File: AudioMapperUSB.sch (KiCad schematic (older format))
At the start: 98 parts, among them J1 USB_B, J10 Conn_01x01, J11 Conn_01x01, J2 Audio-Jack-2, J3 Conn_01x02, J4 Audio-Jack-2, J5 Conn_01x02, J6 Conn_01x02, J7 Conn_01x02, J8 Conn_01x01, J9 Conn_01x01, Q1 SS8550, U1 AMS1117-3.3, U2 PCM2900, U3 OPA2170, U4 OPA2170, U5 OPA2170, Y1 12 MHz

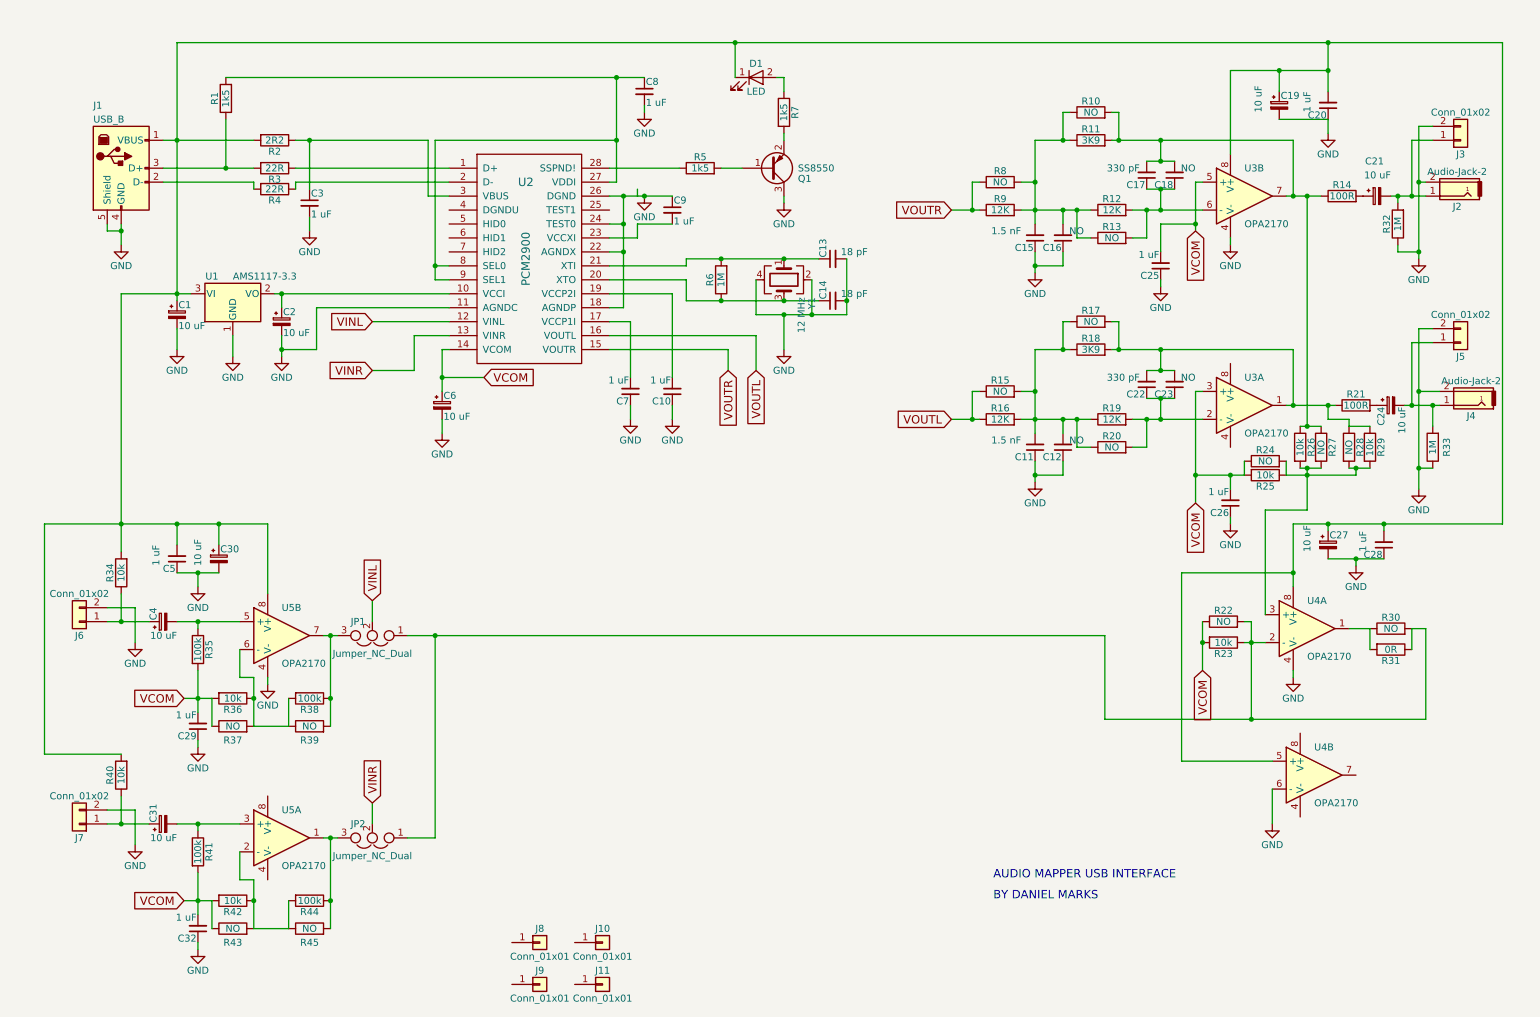
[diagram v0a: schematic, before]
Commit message: Added second gain stage to microphone
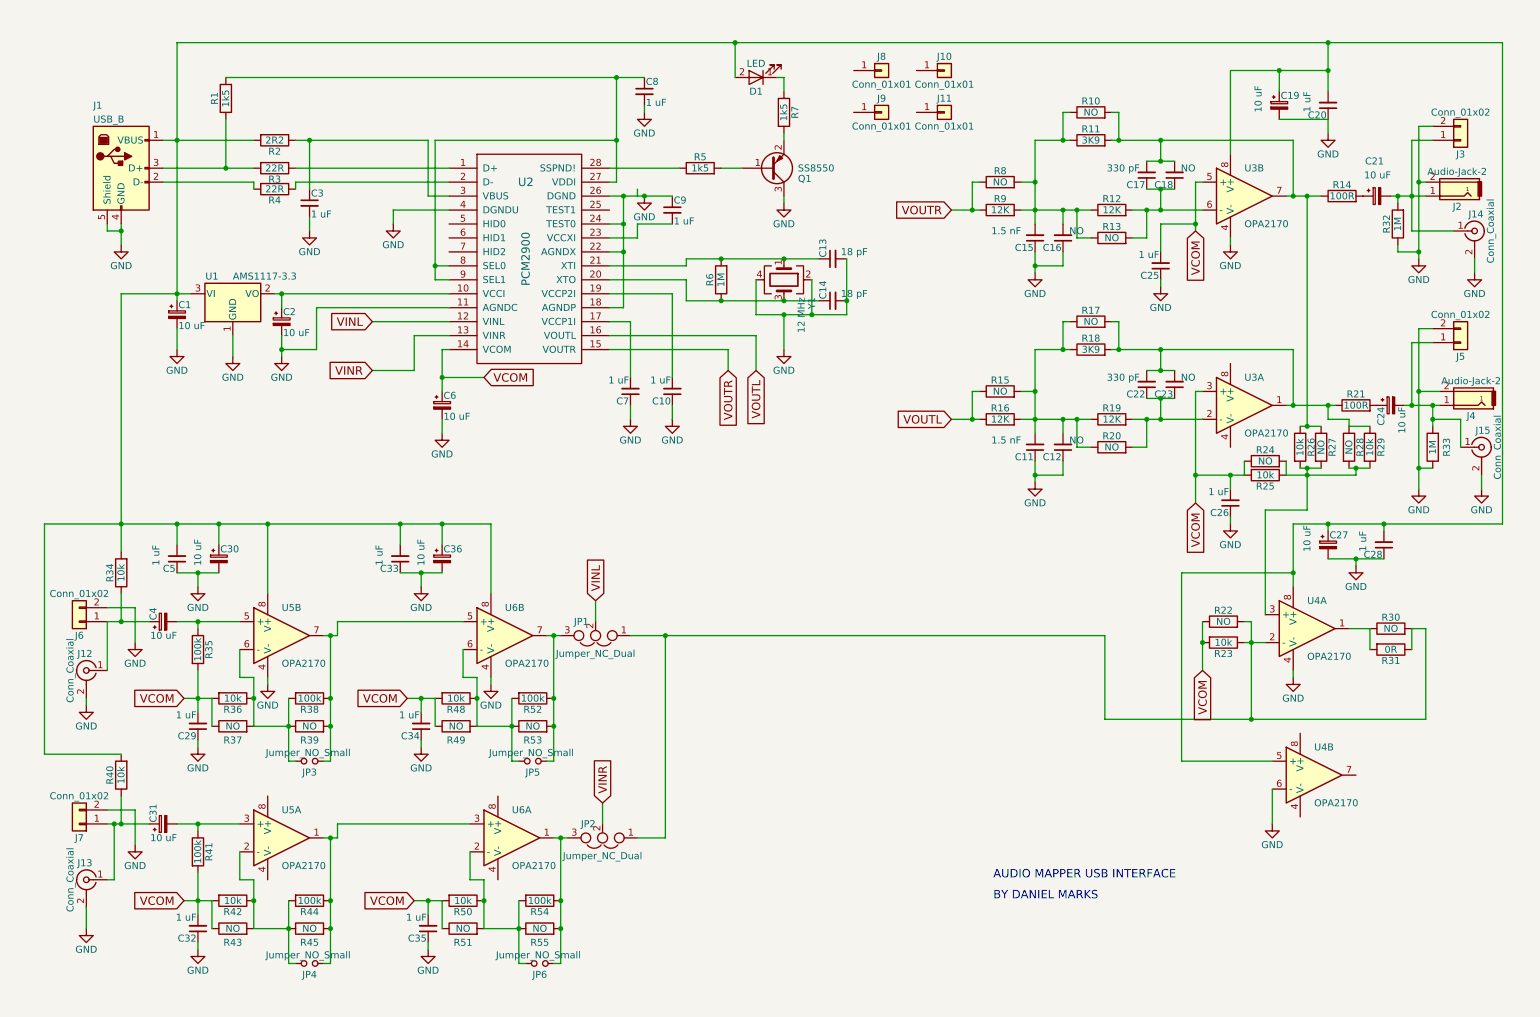
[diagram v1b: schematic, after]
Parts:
- added C33, C34, C35: 1 uF, Capacitors_SMD:C_0805_HandSoldering, symbol C_Small
- added C36: 10 uF, AudioMapperUSB:CP_1206_HandSoldering, symbol CP_Small
- added J12, J13, J14, J15: Conn_Coaxial, Connectors:SMA_THT_Jack_Straight, symbol Conn_Coaxial
- added JP3, JP4, JP5, JP6: Jumper_NO_Small, Pin_Headers:Pin_Header_Straight_1x02_Pitch2.54mm, symbol Jumper_NO_Small
- added R48, R50: 10k, Resistors_SMD:R_0805_HandSoldering, symbol R
- added R49, R51, R53, R55: NO, Resistors_THT:R_Axial_DIN0207_L6.3mm_D2.5mm_P7.62mm_Horizontal, symbol R
- added R52, R54: 100k, Resistors_SMD:R_0805_HandSoldering, symbol R
- added U6: OPA2170, Housings_SOIC:SOIC-8_3.9x4.9mm_Pitch1.27mm, symbol LM358
- C1, C19, C2, C21, C24, C27, C30, C31, C4, C6: footprint Capacitors_SMD:C_1206_HandSoldering -> AudioMapperUSB:CP_1206_HandSoldering
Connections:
- net GND: now also U2.4 (DGNDU), C33.1, C34.1, C35.1, C36.2, J12.2 (Ext), J13.2 (Ext), J14.2 (Ext), J15.2 (Ext), U6.4 (V-)
- net VCOM: now also C34.2, C35.2, R48.2, R49.1, R50.2, R51.1
- net at C1.1, C19.1, C20.2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: now also D1.2 (A), C33.2, C36.1, U6.8 (V+); no longer D1.1 (K)
- net at C4.1, J6.1 (Pin_1), R34.1: now also J12.1 (In)
- net at C24.2, J4.1, J5.1 (Pin_1)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: now also J15.1 (In)
- net at C21.2, J2.1, J3.1 (Pin_1)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: now also J14.1 (In)
- net at R7.1: now also D1.1 (K); no longer D1.2 (A)
- net at R36.1, R37.2, R38.2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: now also JP3.2
- net at R38.1, R39.2, U5.7: now also JP3.1, U6.5 (+); no longer JP1.3
- net at C31.1, J7.1 (Pin_1), R40.1: now also J13.1 (In)
- net at R44.1, R45.2, U5.1: now also JP4.1, U6.3 (+); no longer JP2.3
- net at R42.1, R43.2, R44.2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: now also JP4.2
- new net: JP1.3, JP5.1, R52.1, R53.2, U6.7
- new net: JP2.3, JP6.1, R54.1, R55.2, U6.1
- new net: JP6.2, R50.1, R51.2, R54.2, R55.1, U6.2 (-)
- new net: JP5.2, R48.1, R49.2, R52.2, R53.1, U6.6 (-)
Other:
- moved on the sheet: D1, J10, J11, J8, J9, JP1, JP2

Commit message: Added antialiasing on input and SP/DIF input/output
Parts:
- added C37, C38, C39, C40: 22 pF, Capacitors_SMD:C_0805_HandSoldering, symbol C_Small
- added J16, J17: Audio-Jack-2, AudioMapperUSB:RCAConnectorCommon, symbol Audio-Jack-2
- added JP7: Jumper_NC_Small, Pin_Headers:Pin_Header_Straight_1x02_Pitch2.54mm, symbol Jumper_NC_Small
- R11: value 3K9 -> 12K; LCSC C17614 -> C17444
- R12, R19: value 12K -> 3k9; LCSC C17444 -> C17614
- R18: value 3K9 -> 12K
- R36, R42, R48, R50: value 10k -> 4k7; LCSC C17414 -> C17673
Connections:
- net GND: now also C9.2, J16.2, J17.2, JP7.1; no longer C9.1, U2.24 (TEST0)
- net at U2.23 (VCCXI): now also C9.1; no longer C9.2
- net at U2.25 (TEST1): now also J16.1
- net at JP3.2, R36.1, R37.2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: now also C37.1
- net at JP3.1, R38.1, R39.2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: now also C37.2
- net at JP1.3, JP5.1, R52.1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: now also C39.2
- net at JP4.1, R44.1, R45.2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: now also C38.2
- net at JP4.2, R42.1, R43.2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: now also C38.1
- net at JP2.3, JP6.1, R54.1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: now also C40.2
- net at JP6.2, R50.1, R51.2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: now also C40.1
- net at JP5.2, R48.1, R49.2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: now also C39.1
- new net: J17.1, JP7.2, U2.24 (TEST0)
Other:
- moved on the sheet: C9, D1, Q1, R5, R7

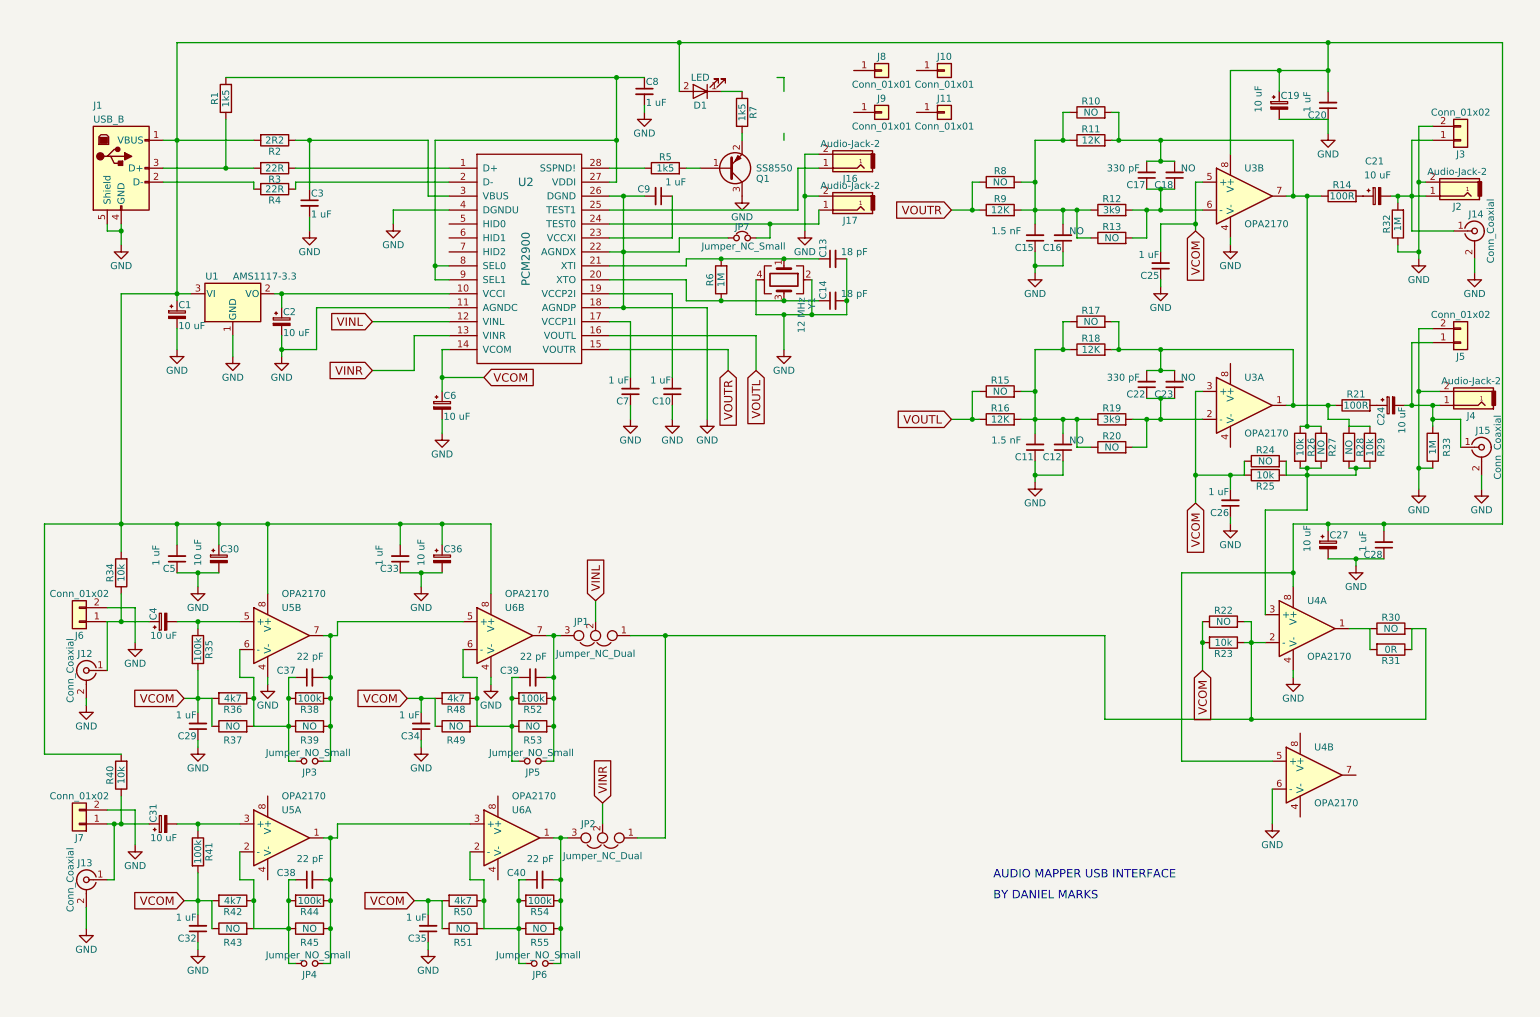
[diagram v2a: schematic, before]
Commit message: Added ability to chain outputs of two boards together
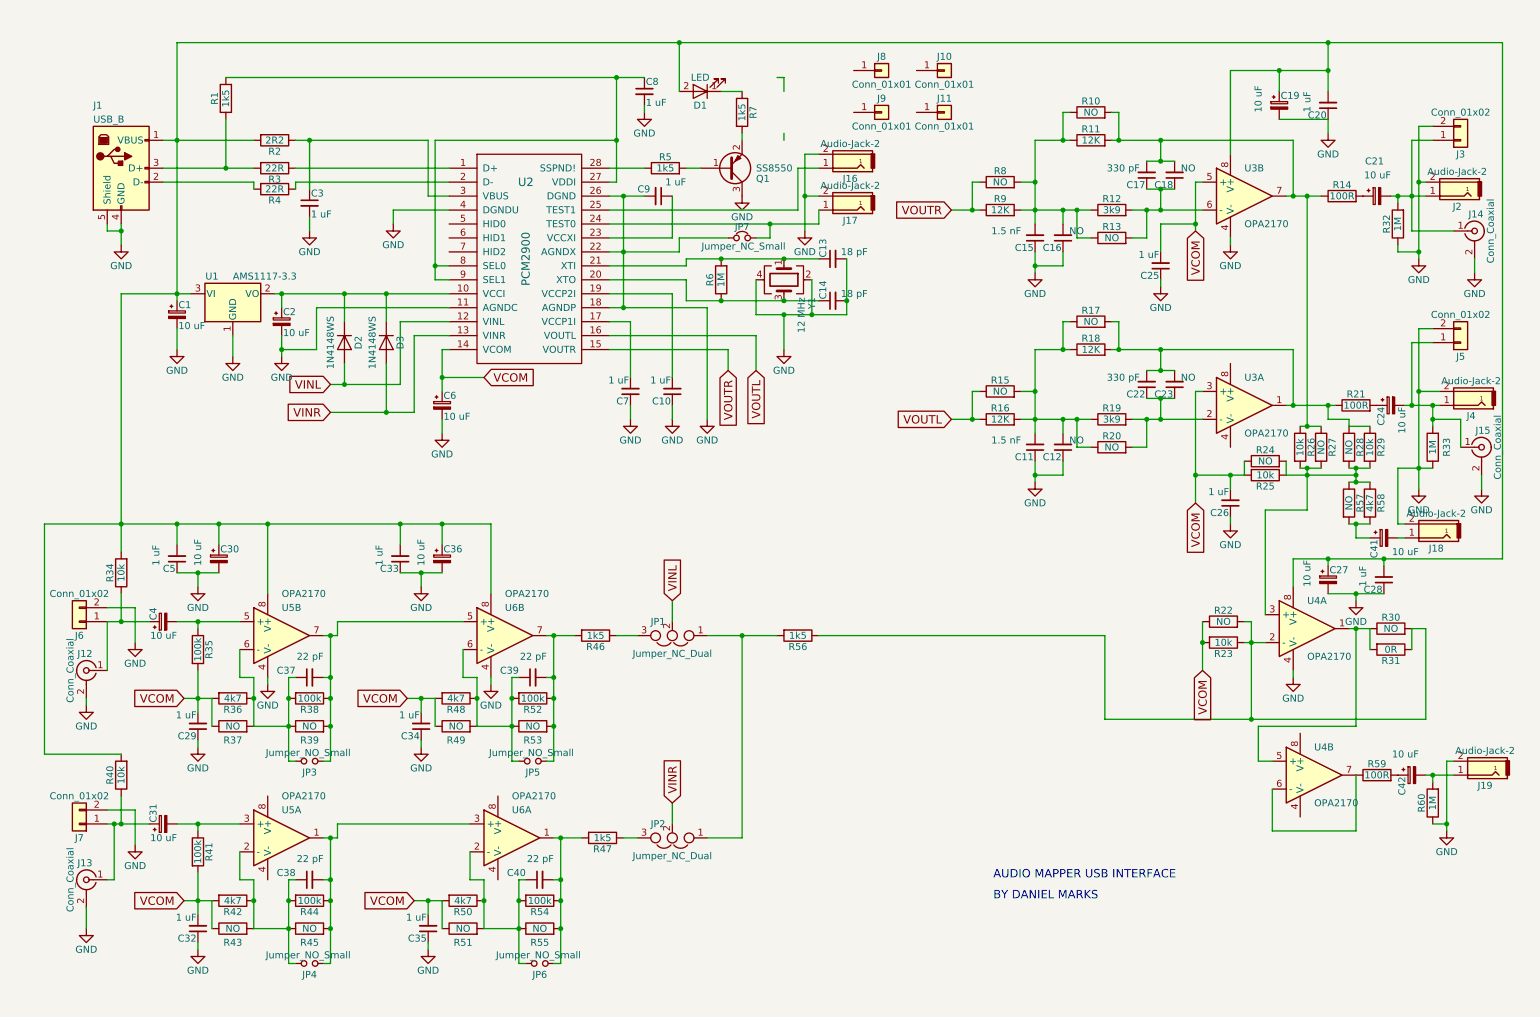
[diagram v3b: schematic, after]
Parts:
- added C41, C42: 10 uF, AudioMapperUSB:CP_1206_HandSoldering, symbol CP_Small
- added D2, D3: 1N4148WS, Diodes_SMD:D_SOD-323_HandSoldering, symbol D
- added J18, J19: Audio-Jack-2, AudioMapperUSB:RCAConnectorCommon, symbol Audio-Jack-2
- added R46, R47, R56: 1k5, Resistors_SMD:R_0805_HandSoldering, symbol R
- added R57: NO, Resistors_THT:R_Axial_DIN0207_L6.3mm_D2.5mm_P7.62mm_Horizontal, symbol R
- added R58: 4k7, Resistors_SMD:R_0805_HandSoldering, symbol R
- added R59: 100R, Resistors_SMD:R_0805_HandSoldering, symbol R
- added R60: 1M, Resistors_SMD:R_0805_HandSoldering, symbol R
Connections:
- net GND: now also J18.2, J19.2, R60.1; no longer U4.6 (-)
- net VINL: now also D2.2 (A)
- net VINR: now also D3.2 (A)
- net at C2.1, U1.2 (VO), U2.10 (VCCI): now also D2.1 (K), D3.1 (K)
- net at C1.1, C19.1, C20.2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: no longer U4.5 (+)
- net at U4.7: now also U4.6 (-), R59.1
- net at R30.1, R31.2, U4.1: now also U4.5 (+)
- net at R22.2, R23.1, R30.2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: now also R56.1; no longer JP1.1, JP2.1
- net at R24.2, R25.1, R26.2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: now also R57.1, R58.1
- net at C39.2, JP5.1, R52.1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: now also R46.2; no longer JP1.3
- net at C40.2, JP6.1, R54.1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: now also R47.2; no longer JP2.3
- new net: JP1.1, JP2.1, R56.2
- new net: JP1.3, R46.1
- new net: JP2.3, R47.1
- new net: C41.2, J18.1
- new net: C41.1, R57.2, R58.2
- new net: C42.2, J19.1, R60.2
- new net: C42.1, R59.2
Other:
- moved on the sheet: C27, C28, JP1, JP2

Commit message: Added real circuit to interface SPDIF levels to 3.3 V CMOS levels
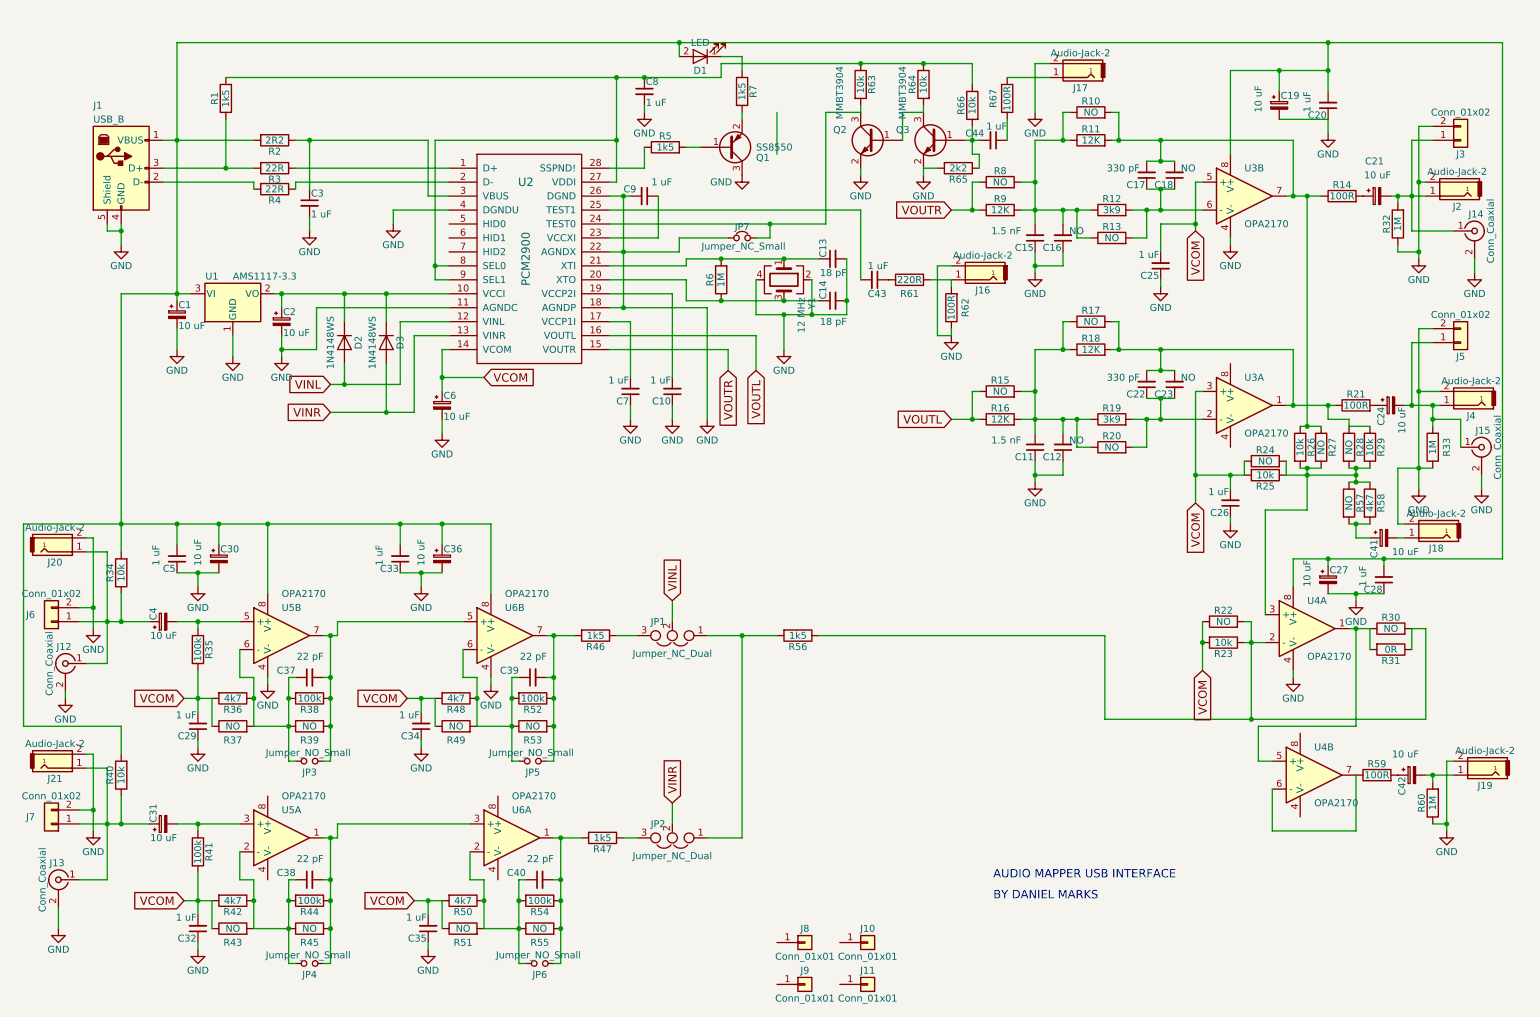
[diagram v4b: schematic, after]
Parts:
- added C43, C44: 1 uF, Capacitors_SMD:C_0805_HandSoldering, symbol C_Small
- added J20, J21: Audio-Jack-2, AudioMapperUSB:RCAConnectorCommon, symbol Audio-Jack-2
- added Q2, Q3: MMBT3904, TO_SOT_Packages_SMD:SOT-23, symbol MMBT3904
- added R61: 220R, Resistors_SMD:R_0805_HandSoldering, symbol R
- added R62, R67: 100R, Resistors_SMD:R_0805_HandSoldering, symbol R
- added R63, R64, R66: 10k, Resistors_SMD:R_0805_HandSoldering, symbol R
- added R65: 2k2, Resistors_SMD:R_0805_HandSoldering, symbol R
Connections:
- net GND: now also J20.2, J21.2, Q2.2 (E), Q3.2 (E), R62.1, R65.2
- net at JP7.2, U2.24 (TEST0): now also Q2.3 (C), R63.2; no longer J17.1
- net at U2.25 (TEST1): now also C43.2; no longer J16.1
- net at C8.1, R1.2, U2.27 (VDDI)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: now also R63.1, R64.1, R66.1
- net at C4.1, J12.1 (In), J6.1 (Pin_1)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: now also J20.1
- net at C31.1, J13.1 (In), J7.1 (Pin_1)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: now also J21.1
- new net: J16.1, R61.2, R62.2
- new net: J17.1, R67.1
- new net: C43.1, R61.1
- new net: C44.2, Q3.1 (B), R65.1, R66.2
- new net: Q2.1 (B), Q3.3 (C), R64.2
- new net: C44.1, R67.2
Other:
- moved on the sheet: C9, D1, J10, J11, J12, J13, J16, J17, J6, J7, J8, J9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

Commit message: Added pulldown resistor to input
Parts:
- added R68: 100R, Resistors_SMD:R_0805_HandSoldering, symbol R
- R67: value 100R -> 220R; LCSC C17408 -> 220R
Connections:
- net GND: now also R68.2
- net at J17.1, R67.1: now also R68.1
